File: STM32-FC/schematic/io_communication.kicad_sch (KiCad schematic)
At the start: 17 parts, among them J11 GH 1.25mm 6P, J12 GH 1.25mm 6P, J13 GH 1.25mm 4P, J14 GH 1.25mm 4P, J15 GH 1.25mm 4P, U10 ATA6561-GBQW, U11 ATA6561-GBQW

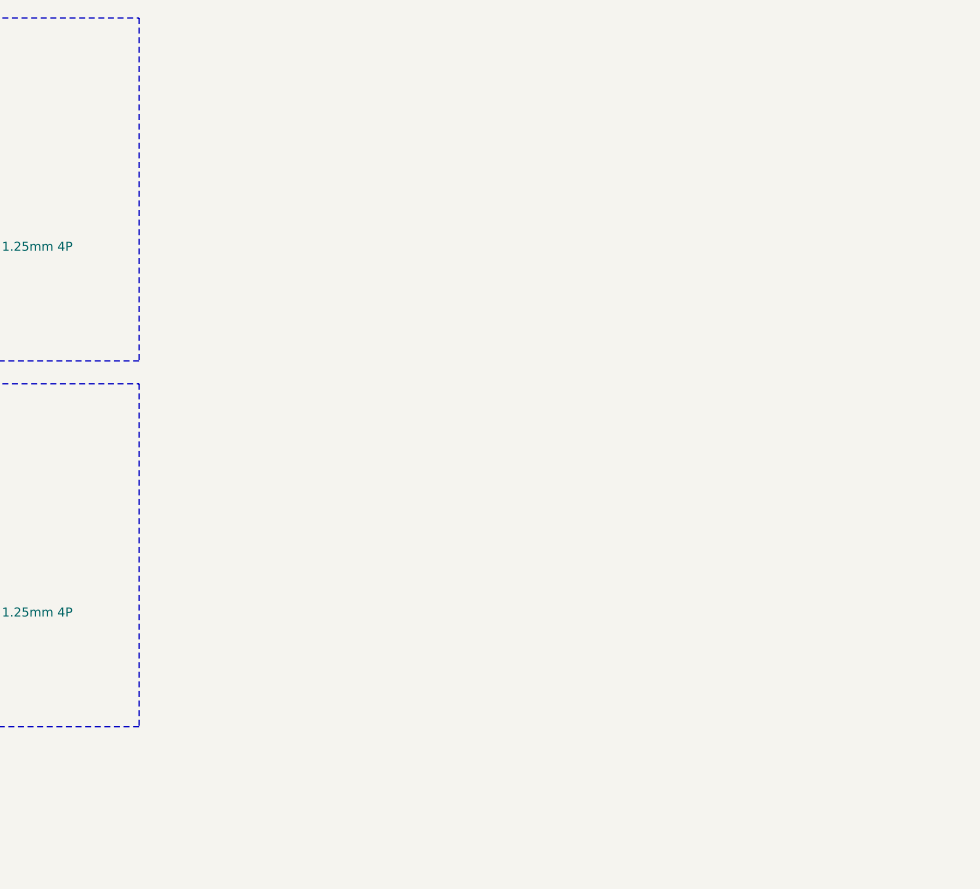
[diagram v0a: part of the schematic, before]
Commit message: v1.0.1 update WIP
repactor and USB C bug fix
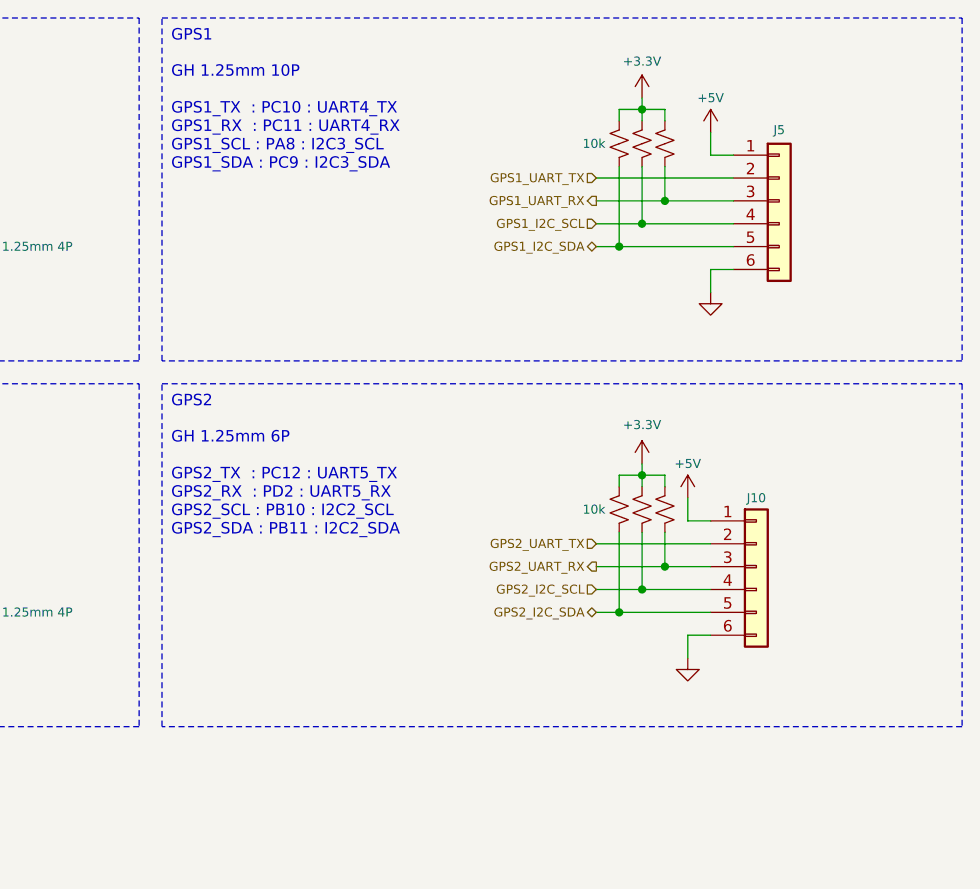
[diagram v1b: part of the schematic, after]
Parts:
- added J10, J5: GH 1.25mm 6P, JST_GH:JST_GH_SM06B-GHS-TB_06x1.25mm_Angled, symbol Connector_Generic:Conn_01x06
- added R23, R24, R25, R26, R27, R28: 10k, Resistor_SMD:R_0402_1005Metric, symbol Device:R_Small_US
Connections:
- net +3.3V: now also R23.1, R24.1, R25.1, R26.1, R27.1, R28.1
- net +5V: now also J10.1 (Pin_1), J5.1 (Pin_1)
- net GND: now also J10.6 (Pin_6), J5.6 (Pin_6)
- new net GPS1_I2C_SCL: J5.4 (Pin_4), R24.2
- new net GPS1_I2C_SDA: J5.5 (Pin_5), R23.2
- new net GPS1_UART_RX: J5.3 (Pin_3), R26.2
- new net GPS1_UART_TX: J5.2 (Pin_2)
- new net GPS2_I2C_SCL: J10.4 (Pin_4), R27.2
- new net GPS2_I2C_SDA: J10.5 (Pin_5), R25.2
- new net GPS2_UART_RX: J10.3 (Pin_3), R28.2
- new net GPS2_UART_TX: J10.2 (Pin_2)
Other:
- note added: "GH 1.25mm 10P GPS1_TX : PC10 : UART4_TX GPS1_RX : PC11 : UART4_RX GPS1_SCL : PA8 : I2C3_SCL GPS1_SDA : PC9 : I2C3_SDA"
- note added: "GH 1.25mm 6P GPS2_TX : PC12 : UART5_TX GPS2_RX : PD2 : UART5_RX GPS2_SCL : PB10 : I2C2_SCL GPS2_SDA : PB11 : I2C2_SDA"
- note added: "GPS1"
- note added: "GPS2"

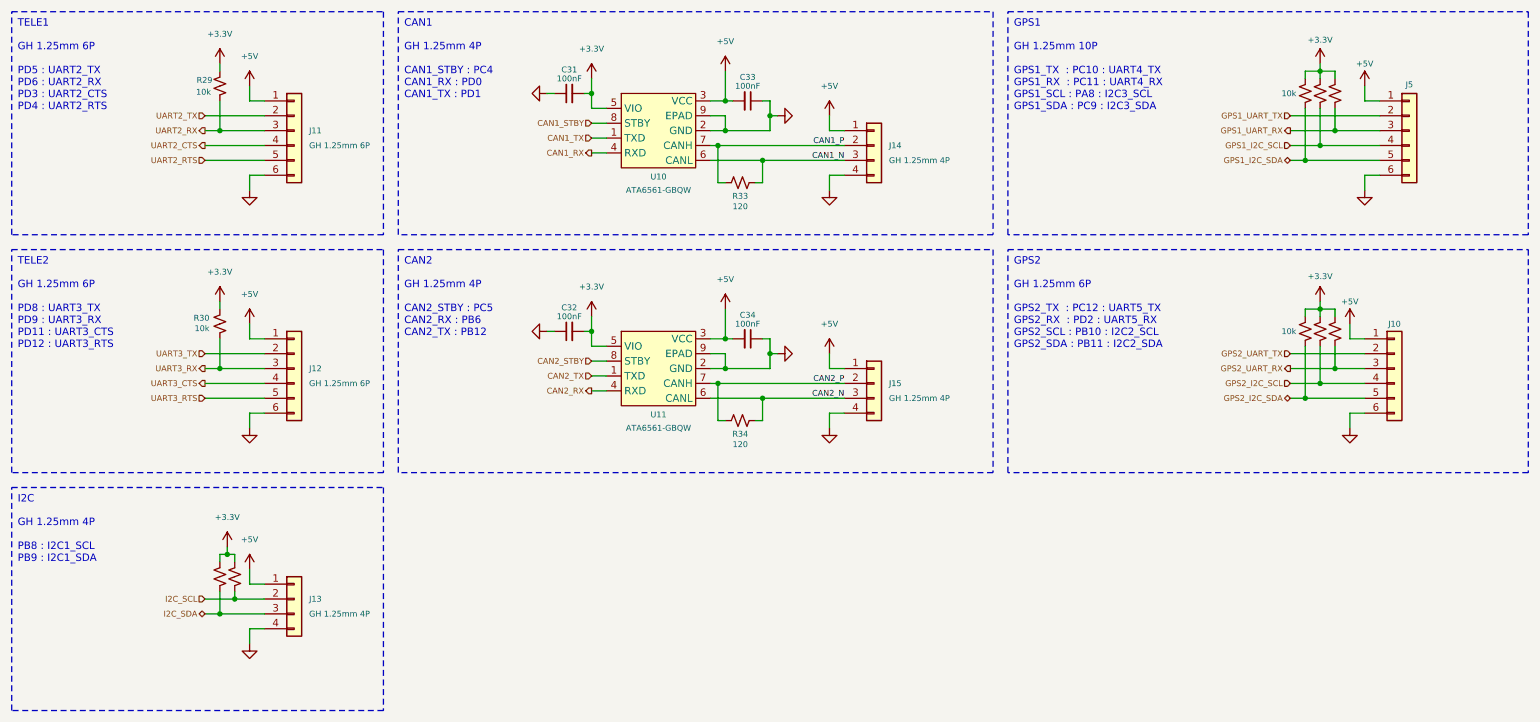
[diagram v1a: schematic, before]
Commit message: schematic update & lib update
- ICM-45686
- ICP-20100
- Micro SD update SDIO instead of SPI
- servo main output
- DC2DC buck instead power regulator
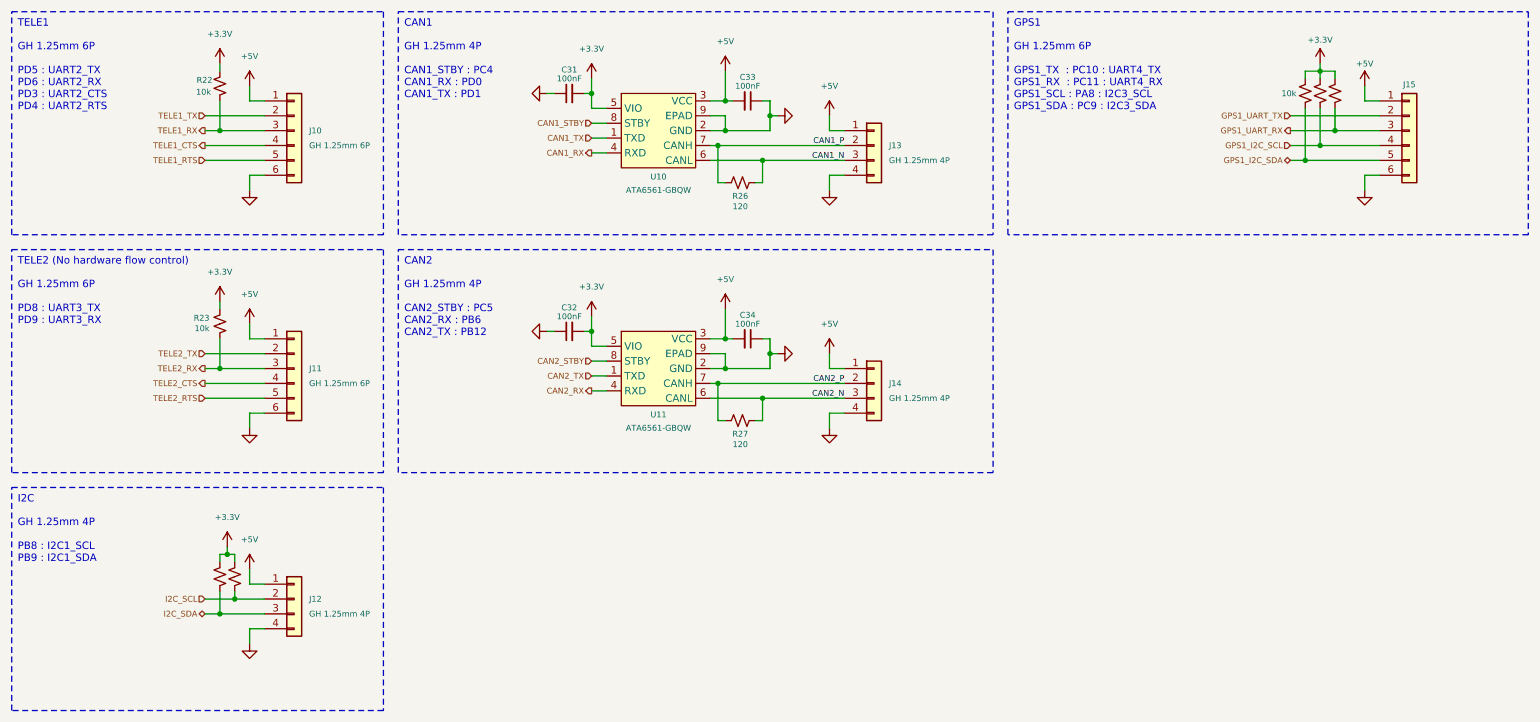
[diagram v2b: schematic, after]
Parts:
- removed J10: GH 1.25mm 6P, JST_GH:JST_GH_SM06B-GHS-TB_06x1.25mm_Angled, symbol Connector_Generic:Conn_01x06
- removed R25, R27, R28: 10k, Resistor_SMD:R_0402_1005Metric, symbol Device:R_Small_US
- J10: renamed from J11; footprint JST_GH:JST_GH_SM06B-GHS-TB_06x1.25mm_Angled -> Connector_JST:JST_GH_BM06B-GHS-TBT_1x06-1MP_P1.25mm_Vertical; LCSC C133065 -> C189892
- J11: renamed from J12; footprint JST_GH:JST_GH_SM06B-GHS-TB_06x1.25mm_Angled -> Connector_JST:JST_GH_BM06B-GHS-TBT_1x06-1MP_P1.25mm_Vertical; LCSC C133065 -> C189892
- J12: renamed from J13; footprint JST_GH:JST_GH_SM04B-GHS-TB_04x1.25mm_Angled -> Connector_JST:JST_GH_BM04B-GHS-TBT_1x04-1MP_P1.25mm_Vertical; LCSC C189895 -> C161692
- J13: renamed from J14; footprint JST_GH:JST_GH_SM04B-GHS-TB_04x1.25mm_Angled -> Connector_JST:JST_GH_BM04B-GHS-TBT_1x04-1MP_P1.25mm_Vertical; LCSC C189895 -> C161692
- J14: renamed from J15; footprint JST_GH:JST_GH_SM04B-GHS-TB_04x1.25mm_Angled -> Connector_JST:JST_GH_BM04B-GHS-TBT_1x04-1MP_P1.25mm_Vertical; LCSC C189895 -> C161692
- J15: renamed from J5; footprint JST_GH:JST_GH_SM06B-GHS-TB_06x1.25mm_Angled -> Connector_JST:JST_GH_BM06B-GHS-TBT_1x06-1MP_P1.25mm_Vertical; LCSC C133065 -> C189892
- renumbered R29 to R22, R30 to R23, R31 to R24, R32 to R25, R33 to R26, R34 to R27, R23 to R28, R24 to R29, R26 to R30
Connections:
- net UART2_CTS renamed TELE1_CTS
- net UART2_RTS renamed TELE1_RTS
- net UART2_RX renamed TELE1_RX
- net UART2_TX renamed TELE1_TX
- net UART3_CTS renamed TELE2_CTS
- net UART3_RTS renamed TELE2_RTS
- net UART3_RX renamed TELE2_RX
- net UART3_TX renamed TELE2_TX
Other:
- note added: "GH 1.25mm 6P GPS1_TX : PC10 : UART4_TX GPS1_RX : PC11 : UART4_RX GPS1_SCL : PA8 : I2C3_SCL GPS1_SDA : PC9 : I2C3_SDA"
- note added: "GH 1.25mm 6P PD8 : UART3_TX PD9 : UART3_RX"
- note added: "TELE2 (No hardware flow control)"
- note removed: "GH 1.25mm 10P GPS1_TX : PC10 : UART4_TX GPS1_RX : PC11 : UART4_RX GPS1_SCL : PA8 : I2C3_SCL GPS1_SDA : PC9 : I2C3_SDA"
- note removed: "GH 1.25mm 6P GPS2_TX : PC12 : UART5_TX GPS2_RX : PD2 : UART5_RX GPS2_SCL : PB10 : I2C2_SCL GPS2_SDA : PB11 : I2C2_SDA"
- note removed: "GH 1.25mm 6P PD8 : UART3_TX PD9 : UART3_RX PD11 : UART3_CTS PD12 : UART3_RTS"
- note removed: "GPS2"
- note removed: "TELE2"
- title: STM32 Flight Controller -> NARAEON - Flight Controller

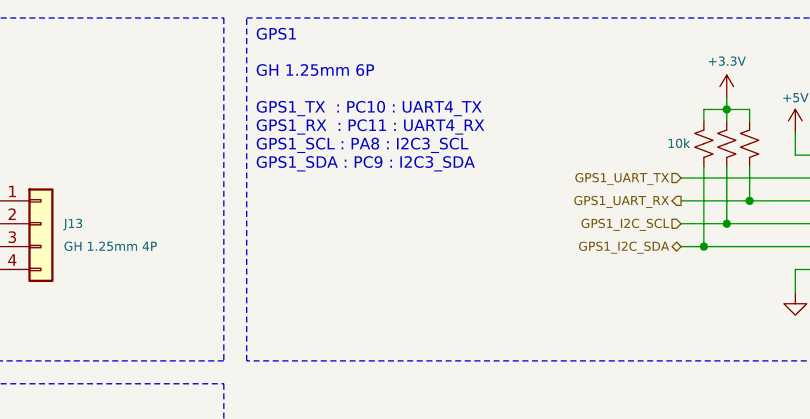
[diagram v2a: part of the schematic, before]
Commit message: add: servo power & comment
- Servo power diode add
- comment update
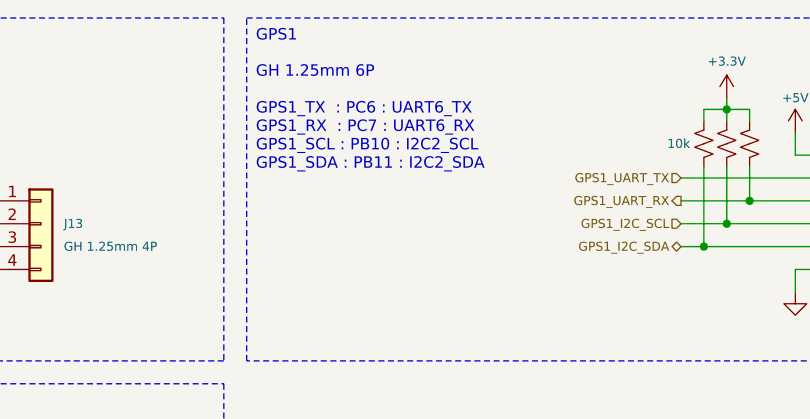
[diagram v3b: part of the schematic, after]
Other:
- note added: "GH 1.25mm 6P GPS1_TX : PC6 : UART6_TX GPS1_RX : PC7 : UART6_RX GPS1_SCL : PB10 : I2C2_SCL GPS1_SDA : PB11 : I2C2_SDA"
- note removed: "GH 1.25mm 6P GPS1_TX : PC10 : UART4_TX GPS1_RX : PC11 : UART4_RX GPS1_SCL : PA8 : I2C3_SCL GPS1_SDA : PC9 : I2C3_SDA"
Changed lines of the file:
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@@
 	(title_block
 		(title "NARAEON - Flight Controller")
-		(date "2025-10-09")
+		(date "2025-10-10")
 		(rev "v1.1.0")
 		(company "NARAE")
@@
 		)
 	)
-	(text "GH 1.25mm 6P\n\nGPS1_TX  : PC10 : UART4_TX\nGPS1_RX  : PC11 : UART4_RX\nGPS1_SCL : PA8 : I2C3_SCL\nGPS1_SDA : PC9 : I2C3_SDA"
+	(text "GH 1.25mm 6P\n\nGPS1_TX  : PC6 : UART6_TX\nGPS1_RX  : PC7 : UART6_RX\nGPS1_SCL : PB10 : I2C2_SCL\nGPS1_SDA : PB11 : I2C2_SDA"
 		(exclude_from_sim no)
 		(at 194.056 18.034 0)
@@
 		(dnp no)
 		(fields_autoplaced yes)
-		(property "Reference" "#PWR098"
+		(property "Reference" "#PWR0102"
 			(at 144.78 67.31 0)
 			(effects
@@
 			(project "STM32-FC"
 				(path "/8d4cc317-3933-4aa6-844b-8c5c635e89c7/a2773f19-5d2b-46e4-ac82-0d57be5829df"
-					(reference "#PWR098")
+					(reference "#PWR0102")
 					(unit 1)
 				)
@@
 		(dnp no)
 		(fields_autoplaced yes)
-		(property "Reference" "#PWR092"
+		(property "Reference" "#PWR096"
 			(at 63.5 127 0)
 			(effects
@@
 			(project "STM32-FC"
 				(path "/8d4cc317-3933-4aa6-844b-8c5c635e89c7/a2773f19-5d2b-46e4-ac82-0d57be5829df"
-					(reference "#PWR092")
+					(reference "#PWR096")
 					(unit 1)
 				)
@@
 		(dnp no)
 		(fields_autoplaced yes)
-		(property "Reference" "#PWR090"
+		(property "Reference" "#PWR094"
 			(at 63.5 90.17 0)
 			(effects
@@
 			(project "STM32-FC"
 				(path "/8d4cc317-3933-4aa6-844b-8c5c635e89c7/a2773f19-5d2b-46e4-ac82-0d57be5829df"
-					(reference "#PWR090")
+					(reference "#PWR094")
 					(unit 1)
 				)
@@
 		(dnp no)
 		(fields_autoplaced yes)
-		(property "Reference" "#PWR0107"
+		(property "Reference" "#PWR0111"
 			(at 254 49.53 0)
 			(effects
@@
 			(project "STM32-FC"
 				(path "/8d4cc317-3933-4aa6-844b-8c5c635e89c7/a2773f19-5d2b-46e4-ac82-0d57be5829df"
-					(reference "#PWR0107")
+					(reference "#PWR0111")
 					(unit 1)
 				)
@@
 		(dnp no)
 		(fields_autoplaced yes)
-		(property "Reference" "#PWR0101"
+		(property "Reference" "#PWR0105"
 			(at 162.56 34.29 0)
 			(effects
@@
 			(project "STM32-FC"
 				(path "/8d4cc317-3933-4aa6-844b-8c5c635e89c7/a2773f19-5d2b-46e4-ac82-0d57be5829df"
-					(reference "#PWR0101")
+					(reference "#PWR0105")
 					(unit 1)
 				)
@@
 		(on_board yes)
 		(dnp no)
-		(property "Reference" "#PWR0105"
+		(property "Reference" "#PWR0109"
 			(at 246.38 25.4 0)
 			(effects
@@
 			(project "STM32-FC"
 				(path "/8d4cc317-3933-4aa6-844b-8c5c635e89c7/a2773f19-5d2b-46e4-ac82-0d57be5829df"
-					(reference "#PWR0105")
+					(reference "#PWR0109")
 					(unit 1)
 				)
@@
 		(dnp no)
 		(fields_autoplaced yes)
-		(property "Reference" "#PWR0103"
+		(property "Reference" "#PWR0107"
 			(at 162.56 74.93 0)
 			(effects
@@
 			(project "STM32-FC"
 				(path "/8d4cc317-3933-4aa6-844b-8c5c635e89c7/a2773f19-5d2b-46e4-ac82-0d57be5829df"
-					(reference "#PWR0103")
+					(reference "#PWR0107")
 					(unit 1)
 				)
@@
 		(dnp no)
 		(fields_autoplaced yes)
-		(property "Reference" "#PWR091"
+		(property "Reference" "#PWR095"
 			(at 63.5 111.76 0)
 			(effects
@@
 			(project "STM32-FC"
 				(path "/8d4cc317-3933-4aa6-844b-8c5c635e89c7/a2773f19-5d2b-46e4-ac82-0d57be5829df"
-					(reference "#PWR091")
+					(reference "#PWR095")
 					(unit 1)
 				)
@@
 		(dnp no)
 		(fields_autoplaced yes)
-		(property "Reference" "#PWR095"
+		(property "Reference" "#PWR099"
 			(at 121.92 27.94 0)
 			(effects
@@
 			(project "STM32-FC"
 				(path "/8d4cc317-3933-4aa6-844b-8c5c635e89c7/a2773f19-5d2b-46e4-ac82-0d57be5829df"
-					(reference "#PWR095")
+					(reference "#PWR099")
 					(unit 1)
 				)
@@
 		(dnp no)
 		(fields_autoplaced yes)
-		(property "Reference" "#PWR089"
+		(property "Reference" "#PWR093"
 			(at 63.5 69.85 0)
 			(effects
@@
 			(project "STM32-FC"
 				(path "/8d4cc317-3933-4aa6-844b-8c5c635e89c7/a2773f19-5d2b-46e4-ac82-0d57be5829df"
-					(reference "#PWR089")
+					(reference "#PWR093")
 					(unit 1)
 				)
@@
 		(dnp no)
 		(fields_autoplaced yes)
-		(property "Reference" "#PWR094"
+		(property "Reference" "#PWR098"
 			(at 107.95 67.31 0)
 			(effects
@@
 			(project "STM32-FC"
 				(path "/8d4cc317-3933-4aa6-844b-8c5c635e89c7/a2773f19-5d2b-46e4-ac82-0d57be5829df"
-					(reference "#PWR094")
+					(reference "#PWR098")
 					(unit 1)
 				)
@@
 		(dnp no)
 		(fields_autoplaced yes)
-		(property "Reference" "#PWR0102"
+		(property "Reference" "#PWR0106"
 			(at 162.56 49.53 0)
 			(effects
@@
 			(project "STM32-FC"
 				(path "/8d4cc317-3933-4aa6-844b-8c5c635e89c7/a2773f19-5d2b-46e4-ac82-0d57be5829df"
-					(reference "#PWR0102")
+					(reference "#PWR0106")
 					(unit 1)
 				)
@@
 		(dnp no)
 		(fields_autoplaced yes)
-		(property "Reference" "#PWR086"
+		(property "Reference" "#PWR090"
 			(at 59.69 107.95 0)
 			(effects
@@
 			(project "STM32-FC"
 				(path "/8d4cc317-3933-4aa6-844b-8c5c635e89c7/a2773f19-5d2b-46e4-ac82-0d57be5829df"
-					(reference "#PWR086")
+					(reference "#PWR090")
 					(unit 1)
 				)
@@
 		(dnp no)
 		(fields_autoplaced yes)
-		(property "Reference" "#PWR099"
+		(property "Reference" "#PWR0103"
 			(at 160.02 30.48 0)
 			(effects
@@
 			(project "STM32-FC"
 				(path "/8d4cc317-3933-4aa6-844b-8c5c635e89c7/a2773f19-5d2b-46e4-ac82-0d57be5829df"
-					(reference "#PWR099")
+					(reference "#PWR0103")
 					(unit 1)
 				)
@@
 		(dnp no)
 		(fields_autoplaced yes)
-		(property "Reference" "#PWR0100"
+		(property "Reference" "#PWR0104"
 			(at 160.02 71.12 0)
 			(effects
@@
 			(project "STM32-FC"
 				(path "/8d4cc317-3933-4aa6-844b-8c5c635e89c7/a2773f19-5d2b-46e4-ac82-0d57be5829df"
-					(reference "#PWR0100")
+					(reference "#PWR0104")
 					(unit 1)
 				)
@@
 		(dnp no)
 		(fields_autoplaced yes)
-		(property "Reference" "#PWR096"
+		(property "Reference" "#PWR0100"
 			(at 121.92 68.58 0)
 			(effects
@@
 			(project "STM32-FC"
 				(path "/8d4cc317-3933-4aa6-844b-8c5c635e89c7/a2773f19-5d2b-46e4-ac82-0d57be5829df"
-					(reference "#PWR096")
+					(reference "#PWR0100")
 					(unit 1)
 				)
@@
 		(dnp no)
 		(fields_autoplaced yes)
-		(property "Reference" "#PWR084"
+		(property "Reference" "#PWR088"
 			(at 58.42 25.4 0)
 			(effects
@@
 			(project "STM32-FC"
 				(path "/8d4cc317-3933-4aa6-844b-8c5c635e89c7/a2773f19-5d2b-46e4-ac82-0d57be5829df"
-					(reference "#PWR084")
+					(reference "#PWR088")
 					(unit 1)
 				)
@@
 		(dnp no)
 		(fields_autoplaced yes)
-		(property "Reference" "#PWR0104"
+		(property "Reference" "#PWR0108"
 			(at 162.56 90.17 0)
 			(effects
@@
 			(project "STM32-FC"
 				(path "/8d4cc317-3933-4aa6-844b-8c5c635e89c7/a2773f19-5d2b-46e4-ac82-0d57be5829df"
-					(reference "#PWR0104")
+					(reference "#PWR0108")
 					(unit 1)
 				)
@@
 		(on_board yes)
 		(dnp no)
-		(property "Reference" "#PWR0106"
+		(property "Reference" "#PWR0110"
 			(at 254 29.21 0)
 			(effects
@@
 			(project "STM32-FC"
 				(path "/8d4cc317-3933-4aa6-844b-8c5c635e89c7/a2773f19-5d2b-46e4-ac82-0d57be5829df"
-					(reference "#PWR0106")
+					(reference "#PWR0110")
 					(unit 1)
 				)
@@
 		(dnp no)
 		(fields_autoplaced yes)
-		(property "Reference" "#PWR085"
+		(property "Reference" "#PWR089"
 			(at 58.42 66.04 0)
 			(effects
@@
 			(project "STM32-FC"
 				(path "/8d4cc317-3933-4aa6-844b-8c5c635e89c7/a2773f19-5d2b-46e4-ac82-0d57be5829df"
-					(reference "#PWR085")
+					(reference "#PWR089")
 					(unit 1)
 				)
@@
 		(dnp no)
 		(fields_autoplaced yes)
-		(property "Reference" "#PWR093"
+		(property "Reference" "#PWR097"
 			(at 107.95 26.67 0)
 			(effects
@@
 			(project "STM32-FC"
 				(path "/8d4cc317-3933-4aa6-844b-8c5c635e89c7/a2773f19-5d2b-46e4-ac82-0d57be5829df"
-					(reference "#PWR093")
+					(reference "#PWR097")
 					(unit 1)
 				)
@@
 		(dnp no)
 		(fields_autoplaced yes)
-		(property "Reference" "#PWR097"
+		(property "Reference" "#PWR0101"
 			(at 144.78 26.67 0)
 			(effects
@@
 			(project "STM32-FC"
 				(path "/8d4cc317-3933-4aa6-844b-8c5c635e89c7/a2773f19-5d2b-46e4-ac82-0d57be5829df"
-					(reference "#PWR097")
+					(reference "#PWR0101")
 					(unit 1)
 				)
@@
 		(dnp no)
 		(fields_autoplaced yes)
-		(property "Reference" "#PWR088"
+		(property "Reference" "#PWR092"
 			(at 63.5 49.53 0)
 			(effects
@@
 			(project "STM32-FC"
 				(path "/8d4cc317-3933-4aa6-844b-8c5c635e89c7/a2773f19-5d2b-46e4-ac82-0d57be5829df"
-					(reference "#PWR088")
+					(reference "#PWR092")
 					(unit 1)
 				)
@@
 		(dnp no)
 		(fields_autoplaced yes)
-		(property "Reference" "#PWR087"
+		(property "Reference" "#PWR091"
 			(at 63.5 29.21 0)
 			(effects
@@
 			(project "STM32-FC"
 				(path "/8d4cc317-3933-4aa6-844b-8c5c635e89c7/a2773f19-5d2b-46e4-ac82-0d57be5829df"
-					(reference "#PWR087")
+					(reference "#PWR091")
 					(unit 1)
 				)
